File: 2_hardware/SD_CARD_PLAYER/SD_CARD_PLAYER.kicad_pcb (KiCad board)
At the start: 2 copper layers, 142.5 x 128.5 mm, 101 parts, among them J1 Conn_02x05_Odd_Even, J10 SD_CARD_CONN, J11 Analogue Input Jack, J12 Analogue Input Jack, J2 audio output, J3 Digital Input Jack, J4 Digital Input Jack, J5 Digital Input Jack, J7 Digital Input Jack, Q1 MMBT3904, Q2 MMBT3904, Q3 MMBT3904, Q4 MMBT3904, SW1 SW_Push, SW2 SW_Push, SW3 SW_Push, SW4 SW_Push, SW5 SW_SPDT, U1 TL431DBZ, U2 PICO_RP2040, U3 74HC595, U4 MCP6232, U5 LM1117MP-5.0, U6 MCP6002-xMS

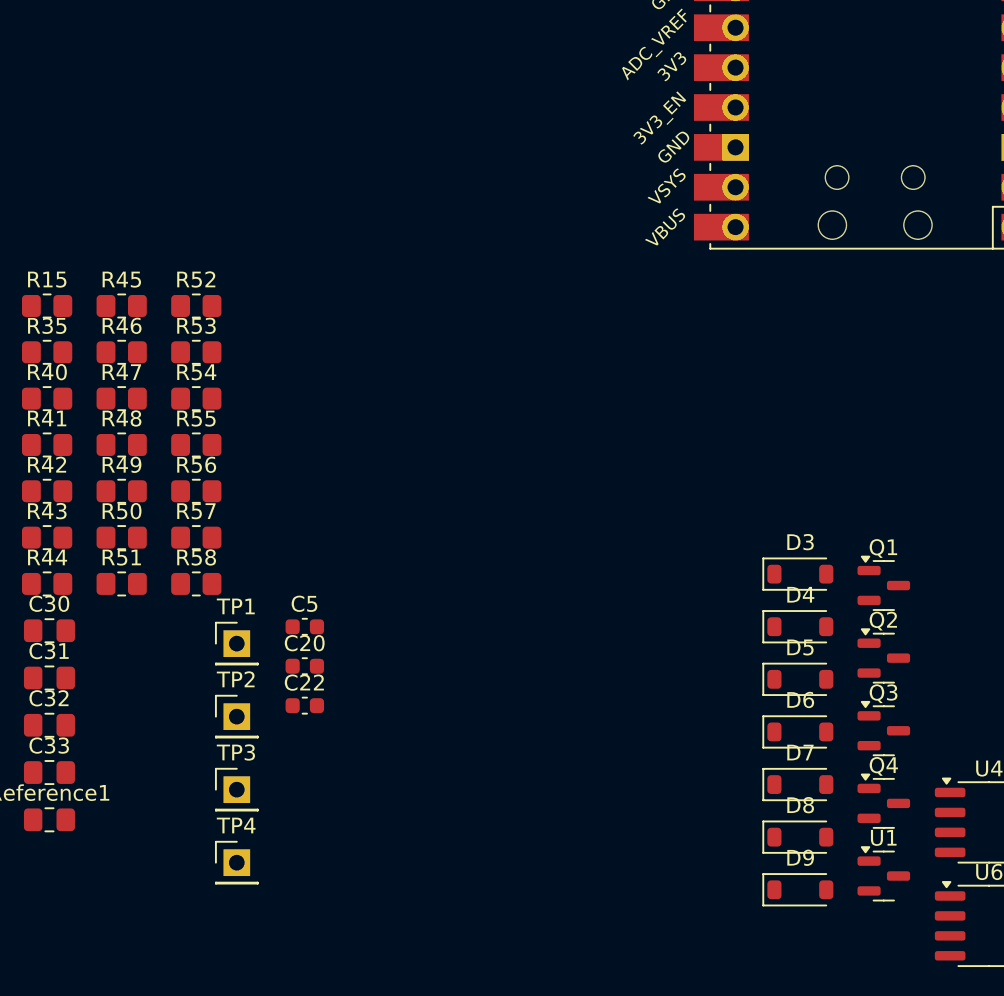
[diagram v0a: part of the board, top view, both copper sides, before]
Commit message: Corrected -vref supply schematic, assigned correct footprint to lm4040B10
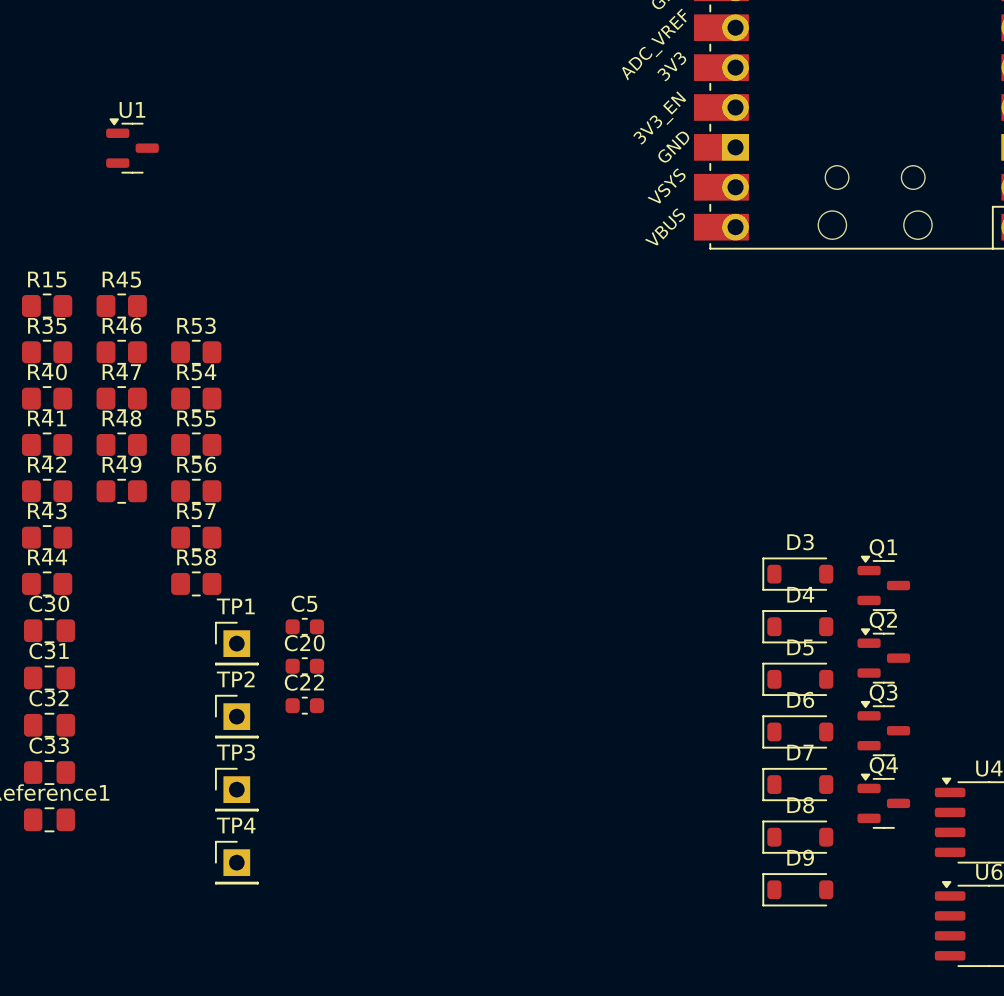
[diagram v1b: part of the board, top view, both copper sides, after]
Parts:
- removed R50: 1k, Resistor_SMD:R_0805_2012Metric_Pad1.20x1.40mm_HandSolder
- removed R51: 2.7k, Resistor_SMD:R_0805_2012Metric_Pad1.20x1.40mm_HandSolder
- removed R52: 8.2k, Resistor_SMD:R_0805_2012Metric_Pad1.20x1.40mm_HandSolder
- C30: value 1uF NP -> 100nF
- U1: value TL431DBZ -> LM4040DBZ-10
- moved U1 66.6 mm to (46.9, 109.0)
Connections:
- C30 pad 1: GND -> -Vref
- C30 pad 2: -Vref -> GND
- U1 pad 2: Net-(U1-REF) -> -Vref
- U1 pad 3: -Vref -> (no net)

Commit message: Update test pcb
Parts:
- moved U2 210.3 mm to (-68.0, -44.0)
